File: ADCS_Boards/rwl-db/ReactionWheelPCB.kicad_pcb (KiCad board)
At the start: 4 copper layers, 90.2 x 95.9 mm, 47 parts, among them J1 PC104_Connector, U1 Conn_1, U10 LM358, U2 Conn_1, U3 Controller 1, U4 Controller 2, U5 Controller 3, U6 Controller 4, U7 Conn_1, U8 Conn_1, U9 LM358

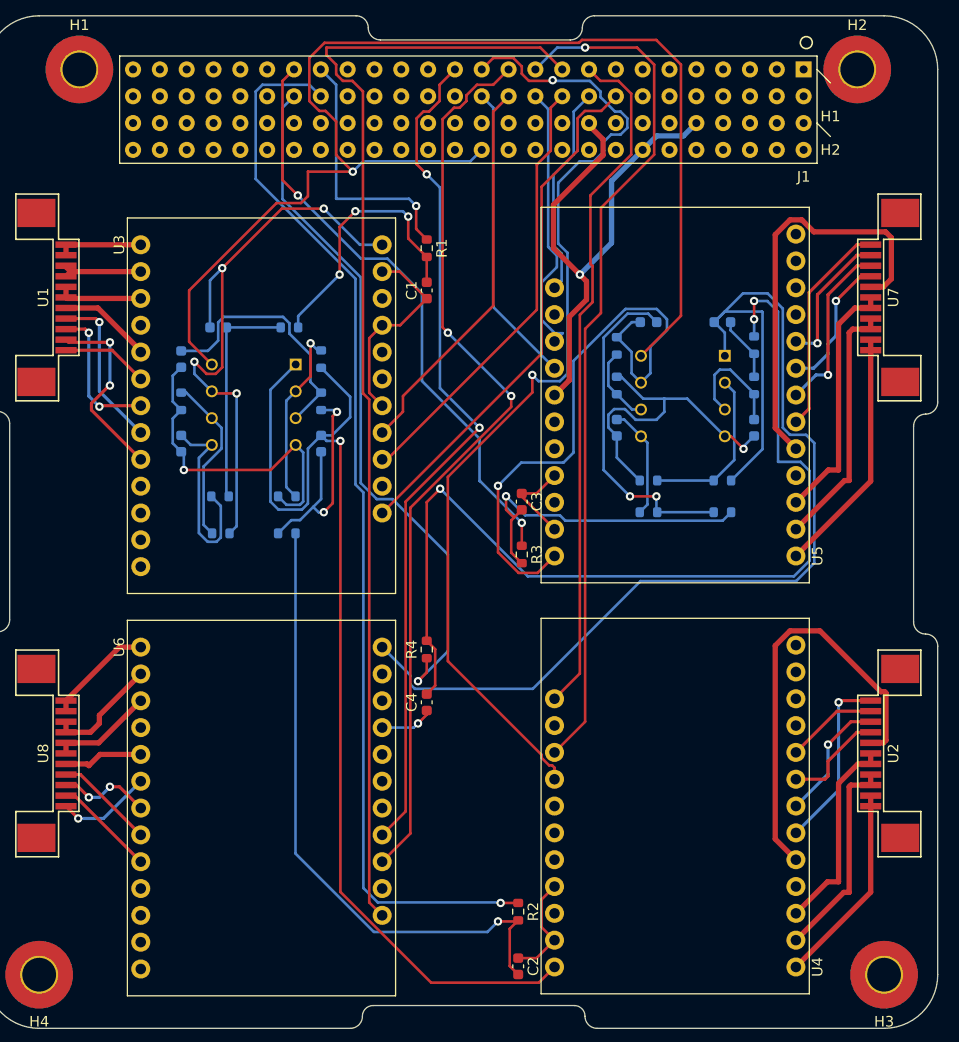
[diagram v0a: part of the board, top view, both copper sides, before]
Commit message: adcs: udpated rwl-db and adcs-ctl on behalf of Yasin
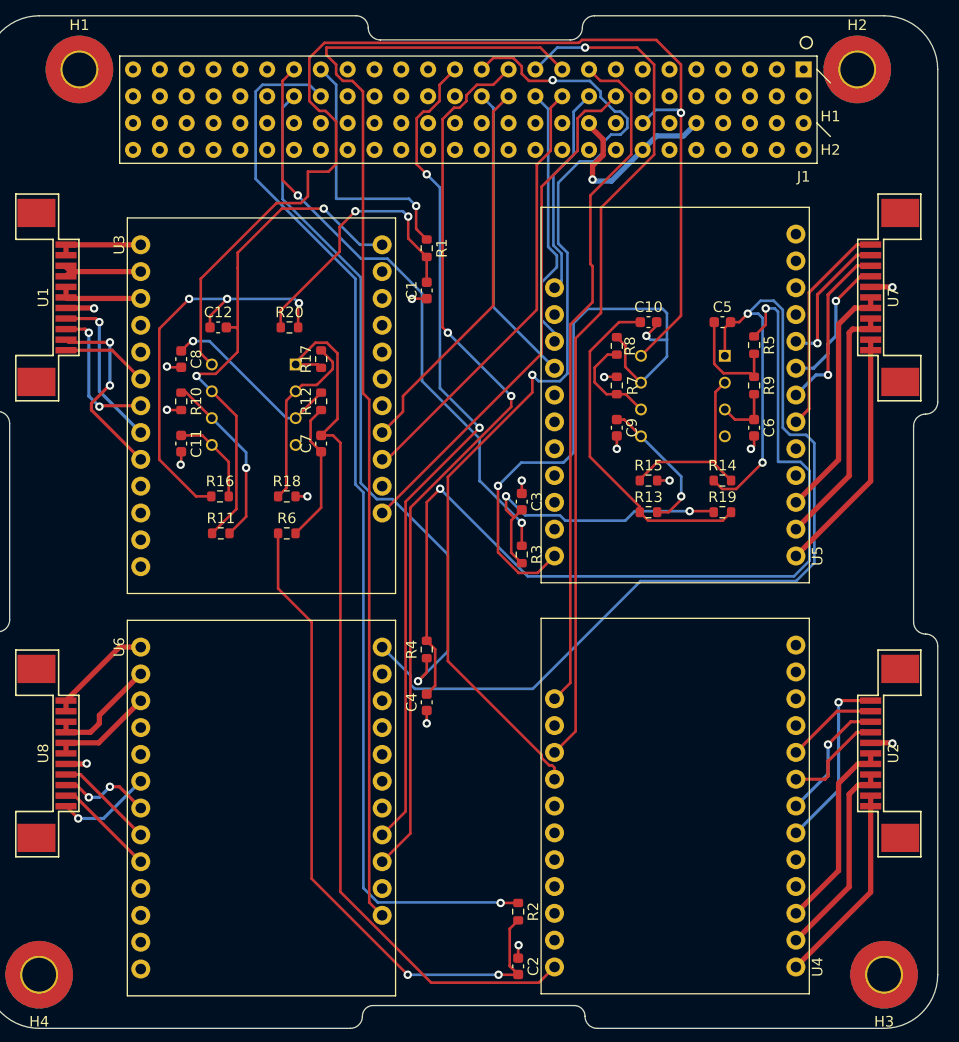
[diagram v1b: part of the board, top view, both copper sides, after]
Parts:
- C1, C2, C3, C4: value 10n -> 10nF
- C10, C11, C12, C5, C6, C7, C8, C9: value C -> 10nF; moved to F.Cu
- R10, R11, R12, R13, R14, R15, R16, R17, R18, R19, R20, R5, R6, R7, R8, R9: value R -> 10k; moved to F.Cu
- turned C10 to 0 degrees
- turned C12 to 0 degrees
- turned C5 to 0 degrees
- turned R11 to 0 degrees
- turned R13 to 0 degrees
- turned R14 to 0 degrees
- turned R15 to 0 degrees
- turned R16 to 0 degrees
- turned R18 to 0 degrees
- turned R19 to 0 degrees
- turned R20 to 0 degrees
- turned R6 to 0 degrees
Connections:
- J1 pad 65: unconnected-(J1-Pad65) -> +5V
- J1 pad 78: +5V -> unconnected-(J1-Pad78)
- J1 pad 79: +3.3V -> unconnected-(J1-Pad79)
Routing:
- net GND: track 253.5 -> 42.9 mm, vias 4 -> 17
- net RampControl(S2)_Out: track 103.5 -> 85.4 mm, vias 1 -> 0
- net Net-(C12-Pad1): track 21.2 -> 39.0 mm, vias 0 -> 3
- net +5V: track 121.3 -> 108.9 mm
- net Net-(C11-Pad1): track 19.0 -> 8.81 mm
- net Net-(C7-Pad1): track 22.7 -> 13.5 mm, vias 2 -> 0
- net RampControl(S1)_Out: track 57.2 -> 49.6 mm, vias 4 -> 2
- net Net-(C8-Pad1): track 24.1 -> 17.7 mm, vias 0 -> 1
- net Net-(C6-Pad1): track 11.0 -> 5.57 mm
- net Net-(C5-Pad1): track 6.10 -> 10.4 mm
- net RampControl(S3)_Out: track 56.6 -> 60.1 mm, vias 1 -> 2
- net RampControl(S4)_Out: track 108.2 -> 104.9 mm, vias 0 -> 2
- net Net-(C9-Pad1): track 10.7 -> 13.3 mm, vias 0 -> 1
- net RampControl(S2)_RC: track 60.7 -> 63.3 mm, vias 1 -> 2
- net Net-(R14-Pad2): track 15.8 -> 18.2 mm
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
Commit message: adcs: rwl-db: finish layout for controllers 3 and 4
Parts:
- removed U10, U9: LM358, Footprints_QSAT:DIP794W45P254L959H508Q8
- removed U7, U8: Conn_1, Footprints_QSAT:FPC_11_SAT_1-84953-1
- added J2: Conn_1, qset-footprints:FPC_11_SAT_1-84953-1, F.Cu at (119.1, 71.9)
- added J3: Conn_2, qset-footprints:FPC_11_SAT_1-84953-1, F.Cu at (190.8, 71.9)
- added J4: Conn_3, qset-footprints:FPC_11_SAT_1-84953-1, F.Cu at (119.1, 117.9)
- added J5: Conn_4, qset-footprints:FPC_11_SAT_1-84953-1, F.Cu at (190.5, 117.6)
- J1: footprint pc104-connector:pc104-connector -> qset-footprints:pc104-connector
- U1: value Conn_1 -> Controller 1; footprint Footprints_QSAT:FPC_11_SAT_1-84953-1 -> qset-footprints:Escon24.2
- U2: value Conn_1 -> Controller 2; footprint Footprints_QSAT:FPC_11_SAT_1-84953-1 -> qset-footprints:Escon24.2
- U3: value Controller 1 -> Controller 3; footprint Footprints_QSAT:Escon24.2 -> qset-footprints:Escon24.2
- U4: value Controller 2 -> Controller 4; footprint Footprints_QSAT:Escon24.2 -> qset-footprints:Escon24.2
- U5: value Controller 3 -> LM358; footprint Footprints_QSAT:Escon24.2 -> qset-footprints:DIP794W45P254L959H508Q8
- U6: value Controller 4 -> LM358; footprint Footprints_QSAT:Escon24.2 -> qset-footprints:DIP794W45P254L959H508Q8
- moved C8 255.2 mm to (383.0, 77.5), turned to 0 degrees
- moved R10 251.3 mm to (379.0, 90.0), turned to 0 degrees
- moved R11 240.2 mm to (370.9, 77.5)
- moved R6 237.9 mm to (375.0, 77.5)
- moved C1 236.0 mm to (387.0, 77.5), turned to 0 degrees
- moved U5 235.3 mm to (403.4, 4.78), turned to 0 degrees
- moved R12 226.0 mm to (366.9, 90.0), turned to 0 degrees
- moved C7 226.0 mm to (366.9, 85.0), turned to 0 degrees
- moved R1 221.0 mm to (370.9, 90.0), turned to 0 degrees
- moved R2 219.8 mm to (375.0, 87.5), turned to 0 degrees
- moved R8 218.0 mm to (387.0, 80.0), turned to 0 degrees
- moved U1 216.4 mm to (331.9, 97.4), turned to 90 degrees
- moved C2 215.0 mm to (366.9, 80.0), turned to 0 degrees
- moved R7 202.0 mm to (370.9, 87.5), turned to 0 degrees
- moved R9 201.0 mm to (383.0, 80.0), turned to 0 degrees
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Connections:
- net RampControl(S1) renamed RampControl(S1)_IN
- net RampControl(S2) renamed RampControl(S2)_IN
- net RampControl(S3) renamed RampControl(S3)_IN
- net RampControl(S4) renamed RampControl(S4)_IN
- C10 pad 2: RampControl(S3)_Out -> GND
- C11 pad 1: Net-(C11-Pad1) -> RampControl(S3)_Out
- C11 pad 2: GND -> Net-(C11-Pad2)
- C12 pad 1: Net-(C12-Pad1) -> RampControl(S4)_Out
- C12 pad 2: RampControl(S1)_Out -> Net-(C12-Pad2)
- C5 pad 1: Net-(C5-Pad1) -> GND
- C5 pad 2: RampControl(S4)_Out -> Net-(C5-Pad2)
- C7 pad 1: Net-(C7-Pad1) -> RampControl(S1)_Out
- C7 pad 2: RampControl(S2)_Out -> Net-(C7-Pad2)
- C8 pad 1: Net-(C8-Pad1) -> RampControl(S2)_Out
- C8 pad 2: GND -> Net-(C8-Pad2)
- C9 pad 1: Net-(C9-Pad1) -> GND
- C9 pad 2: GND -> Net-(C9-Pad2)
- J1 pad 84: GND -> unconnected-(J1-Pad84)
- R11 pad 1: RampControl(S1)_Out -> RampControl(S2)_Out
- R11 pad 2: Net-(R10-Pad1) -> Net-(R11-Pad2)
- R12 pad 1: Net-(C7-Pad1) -> Net-(R11-Pad2)
- R12 pad 2: Net-(C8-Pad1) -> GND
- R13 pad 1: Net-(C10-Pad1) -> Net-(C11-Pad2)
- R13 pad 2: Net-(C9-Pad1) -> RampControl(S3)_RC
- R14 pad 1: RampControl(S4)_Out -> RampControl(S4)_RC
- R14 pad 2: Net-(R14-Pad2) -> Net-(C12-Pad2)
- R15 pad 1: Net-(R14-Pad2) -> Net-(C9-Pad2)
- R15 pad 2: GND -> Net-(C11-Pad2)
- R16 pad 1: Net-(C12-Pad1) -> Net-(C12-Pad2)
- R16 pad 2: Net-(C11-Pad1) -> Net-(C10-Pad1)
- R17 pad 1: RampControl(S2)_Out -> RampControl(S3)_Out
- R19 pad 1: RampControl(S3)_RC -> RampControl(S4)_Out
- R19 pad 2: Net-(C10-Pad1) -> Net-(R19-Pad2)
- R20 pad 1: RampControl(S1)_RC -> Net-(R19-Pad2)
- R20 pad 2: Net-(C12-Pad1) -> GND
- R5 pad 1: RampControl(S4)_RC -> Net-(C7-Pad2)
- R5 pad 2: Net-(C5-Pad1) -> RampControl(S1)_RC
- R6 pad 2: Net-(C7-Pad1) -> Net-(C8-Pad2)
- R7 pad 1: Net-(R7-Pad1) -> Net-(C5-Pad2)
- R7 pad 2: GND -> Net-(C7-Pad2)
- R8 pad 1: RampControl(S3)_Out -> Net-(C8-Pad2)
- R8 pad 2: Net-(R7-Pad1) -> Net-(C6-Pad1)
- R9 pad 1: Net-(C5-Pad1) -> RampControl(S1)_Out
- R9 pad 2: Net-(C6-Pad1) -> Net-(R10-Pad1)
- U1 pad 10: Net-(U1-Pad10) -> unconnected-(U1-Pad10)
- U1 pad 11: Net-(U1-Pad10) -> unconnected-(U1-Pad11)
- U1 pad 4: Net-(U1-Pad4) -> +12V
- U1 pad 7: Net-(U1-Pad6) -> Net-(U1-Pad7)
- U1 pad 9: Net-(U1-Pad8) -> Net-(U1-Pad9)
- U2 pad 10: Net-(U2-Pad10) -> unconnected-(U2-Pad10)
- U2 pad 11: Net-(U2-Pad10) -> unconnected-(U2-Pad11)
- U2 pad 4: Net-(U2-Pad4) -> +12V
- U2 pad 7: Net-(U2-Pad6) -> Net-(U2-Pad7)
- U2 pad 9: Net-(U2-Pad8) -> Net-(U2-Pad9)
- U3 pad 1: Net-(U1-Pad10) -> Net-(U3-Pad1)
- U3 pad 14: Enable(S1) -> Enable(S3)
- U3 pad 16: Direction(S1) -> Direction(S3)
- U3 pad 17: PWM-SetValue(S1) -> PWM-SetValue(S3)
- U3 pad 2: Net-(U1-Pad8) -> Net-(U3-Pad2)
- U3 pad 24: RampControl(S1)_Out -> RampControl(S3)_Out
- U3 pad 3: Net-(U1-Pad6) -> Net-(U3-Pad3)
- U3 pad 6: Net-(U1-Pad1) -> Net-(U3-Pad6)
- U3 pad 7: Net-(U1-Pad3) -> Net-(U3-Pad7)
- U3 pad 8: Net-(U1-Pad4) -> Net-(U3-Pad8)
- U3 pad 9: Net-(U1-Pad2) -> Net-(U3-Pad9)
- U4 pad 1: Net-(U2-Pad10) -> Net-(U4-Pad1)
- U4 pad 14: Enable(S2) -> Enable(S4)
- U4 pad 16: Direction(S2) -> Direction(S4)
- U4 pad 17: PWM-SetValue(S2) -> PWM-SetValue(S4)
- U4 pad 2: Net-(U2-Pad8) -> Net-(U4-Pad2)
- U4 pad 24: RampControl(S2)_Out -> RampControl(S4)_Out
- U4 pad 3: Net-(U2-Pad6) -> Net-(U4-Pad3)
- U4 pad 6: Net-(U2-Pad1) -> Net-(U4-Pad6)
- U4 pad 7: Net-(U2-Pad3) -> Net-(U4-Pad7)
- U4 pad 8: Net-(U2-Pad4) -> Net-(U4-Pad8)
- U4 pad 9: Net-(U2-Pad2) -> Net-(U4-Pad9)
- U5 pad 1: Net-(U5-Pad1) -> RampControl(S1)_Out
- U5 pad 2: Net-(U5-Pad2) -> Net-(R10-Pad1)
- U5 pad 3: Net-(U5-Pad3) -> Net-(C5-Pad2)
- U5 pad 4: +12V -> GND
- U5 pad 5: GND -> Net-(C6-Pad1)
- U5 pad 6: Net-(U5-Pad6) -> Net-(R11-Pad2)
- U5 pad 7: Net-(U5-Pad7) -> RampControl(S2)_Out
- U5 pad 8: Net-(U5-Pad8) -> +5V
- U6 pad 1: Net-(U6-Pad1) -> RampControl(S3)_Out
- U6 pad 2: Net-(U6-Pad2) -> Net-(R17-Pad2)
- U6 pad 3: Net-(U6-Pad3) -> Net-(C9-Pad2)
- U6 pad 4: +12V -> GND
- U6 pad 5: GND -> Net-(C10-Pad1)
- U6 pad 6: Net-(U6-Pad6) -> Net-(R19-Pad2)
- U6 pad 7: Net-(U6-Pad7) -> RampControl(S4)_Out
- U6 pad 8: Net-(U6-Pad8) -> +5V
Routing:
- net +5V: track 108.9 -> 1.18 mm
- net RampControl(S2)_IN: track 101.8 -> 0.00 mm, vias 1 -> 0
- net Enable(S4): track 108.1 -> 10.4 mm
- net PWM-SetValue(S2): track 95.8 -> 0.00 mm, vias 2 -> 0
- net RampControl(S4)_RC: track 90.5 -> 3.03 mm, vias 2 -> 0
- net RampControl(S2)_Out: track 85.4 -> 0.00 mm
- net Direction(S2): track 81.8 -> 0.00 mm, vias 1 -> 0
- net RampControl(S4)_Out: track 104.9 -> 31.6 mm, vias 2 -> 0
- net Direction(S4): track 86.6 -> 17.4 mm, vias 2 -> 0
- net Enable(S2): track 65.4 -> 0.00 mm
- net RampControl(S2)_RC: track 63.3 -> 0.00 mm, vias 2 -> 0
- net PWM-SetValue(S4): track 80.6 -> 21.6 mm, vias 2 -> 0
- net RampControl(S4)_IN: track 66.9 -> 12.5 mm, vias 1 -> 0
- net RampControl(S1)_Out: track 49.6 -> 0.00 mm, vias 2 -> 0
- net Enable(S1): track 49.5 -> 0.00 mm
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
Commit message: adcs: rwl-db: finish layout of controllers 1 and 2
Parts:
- added G***: LOGO, LOGO, F.Cu at (117.3, 94.7)
- moved U5 263.8 mm to (154.9, 93.5)
- moved C1 234.5 mm to (152.6, 70.6), turned to -90 degrees
- moved R9 230.4 mm to (152.6, 80.5), turned to -90 degrees
- moved R8 228.8 mm to (158.2, 82.8), turned to 180 degrees
- moved R10 228.1 mm to (151.1, 80.5), turned to 90 degrees
- moved R5 227.2 mm to (151.9, 72.9)
- moved C5 227.1 mm to (151.9, 84.3)
- moved C8 224.8 mm to (158.2, 74.4)
- moved R1 220.7 mm to (151.1, 70.6), turned to -90 degrees
- moved R7 219.1 mm to (151.9, 82.8), turned to 180 degrees
- moved R2 218.1 mm to (157.5, 70.6), turned to -90 degrees
- moved R6 216.8 mm to (158.2, 72.9)
- moved C7 215.3 mm to (151.9, 74.4), turned to 180 degrees
- moved R11 213.5 mm to (157.5, 80.5), turned to -90 degrees
- moved U1 212.5 mm to (122.1, 64.1)
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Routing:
- net PWM-SetValue(S4): track 21.6 -> 101.8 mm
- net Direction(S1): track 0.00 -> 77.8 mm
- net Enable(S3): track 33.6 -> 110.9 mm, vias 0 -> 1
- net Direction(S4): track 17.4 -> 93.6 mm, vias 0 -> 1
- net Enable(S1): track 0.00 -> 73.1 mm, vias 0 -> 1
- net Enable(S4): track 10.4 -> 80.1 mm, vias 0 -> 1
- net Direction(S3): track 27.4 -> 94.2 mm, vias 0 -> 1
- net RampControl(S3)_IN: track 12.7 -> 75.4 mm, vias 0 -> 1
- net RampControl(S4)_IN: track 12.5 -> 74.8 mm, vias 0 -> 1
- net PWM-SetValue(S3): track 24.0 -> 82.4 mm, vias 0 -> 1
- net PWM-SetValue(S1): track 0.00 -> 50.5 mm
- net PWM-SetValue(S2): track 0.00 -> 47.0 mm, vias 0 -> 1
- net Direction(S2): track 0.00 -> 45.8 mm
- net RampControl(S1)_Out: track 0.00 -> 36.2 mm
- net RampControl(S2)_Out: track 0.00 -> 31.4 mm
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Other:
- board text added: "RWL-DB-REVA"
- board text added: "SN: ___________"
- board text added: "Yasin Shahrami Davis Edward Cal Graham Alex Bartley Aidan Sheedy"

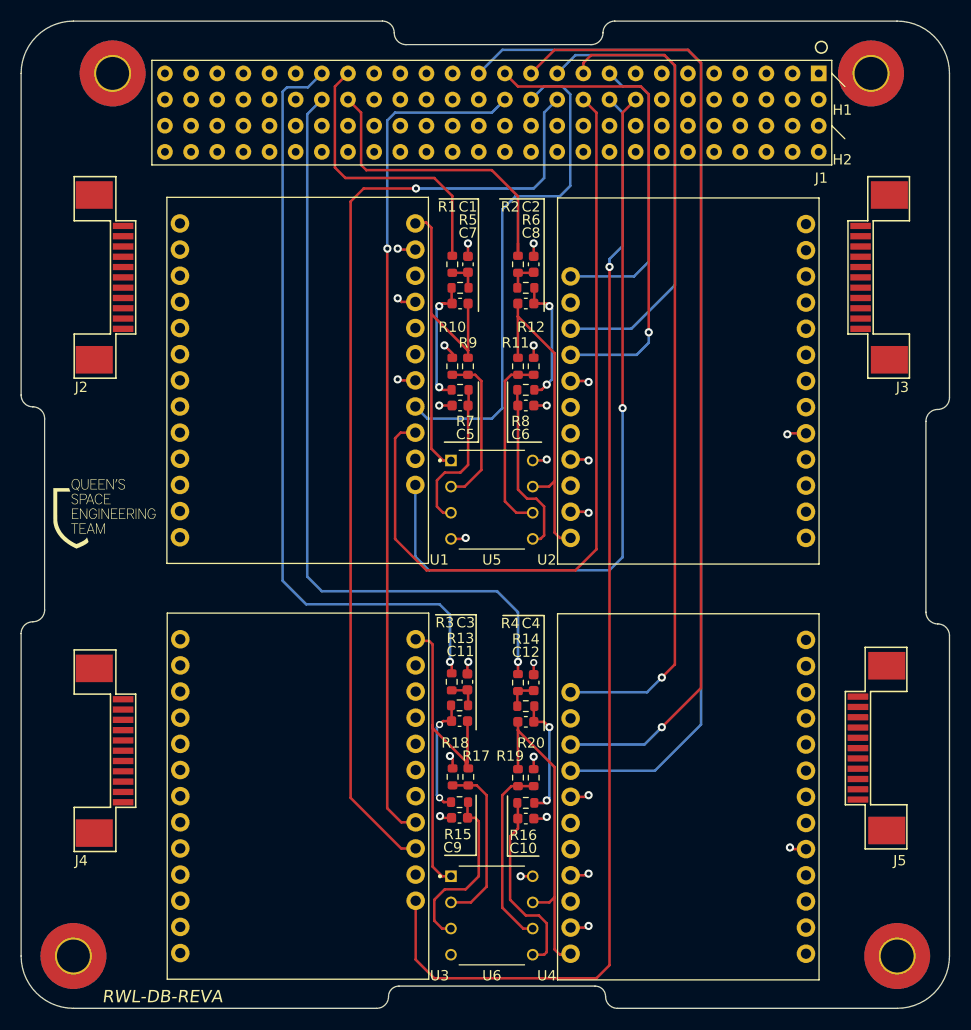
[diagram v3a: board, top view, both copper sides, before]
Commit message: adcs: Updated rw-db with latest PWM filter design and added misc silkscreen
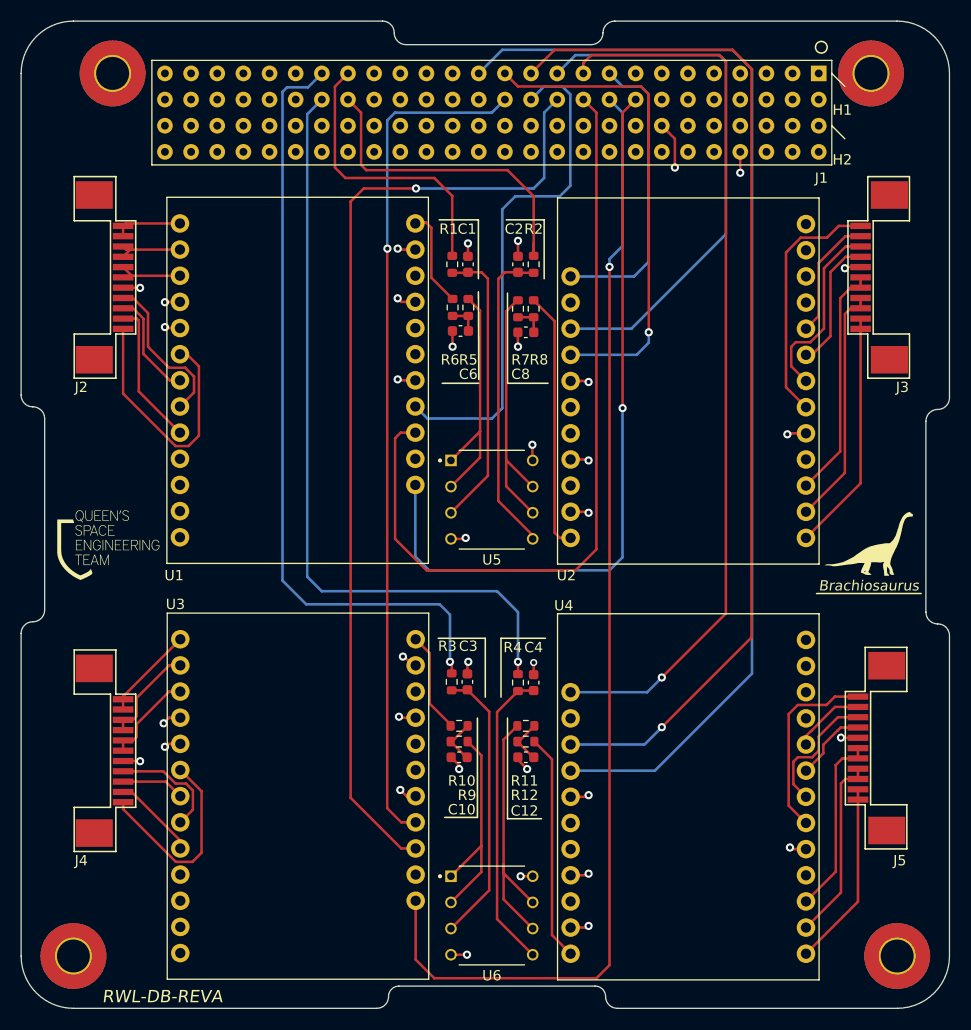
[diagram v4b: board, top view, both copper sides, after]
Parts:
- removed C11, C5, C7, C9: 10nF, Capacitor_SMD:C_0603_1608Metric
- removed R13, R14, R15, R16, R17, R18, R19, R20: 10k, Resistor_SMD:R_0603_1608Metric
- added Brachiosaurus: LOGO, LOGO, F.Cu at (192.3, 97.8)
- moved R9 36.5 mm to (151.8, 117.0), turned to 0 degrees
- moved R12 36.5 mm to (158.2, 117.0), turned to 0 degrees
- moved R11 34.9 mm to (158.2, 115.4), turned to 0 degrees
- moved R10 34.9 mm to (151.8, 115.4), turned to 0 degrees
- moved R7 9.67 mm to (157.5, 74.9), turned to -90 degrees
- moved C6 9.63 mm to (151.9, 77.1)
- moved C10 8.80 mm to (151.8, 118.5)
- moved R8 7.91 mm to (159.0, 74.9), turned to -90 degrees
- moved R6 7.36 mm to (151.1, 74.8), turned to -90 degrees
- moved C12 3.44 mm to (158.2, 118.5)
- moved G*** 3.07 mm to (117.7, 97.8)
- moved C8 2.79 mm to (158.2, 77.2)
- moved R5 2.06 mm to (152.7, 74.8), turned to 90 degrees
- moved C2 1.52 mm to (157.5, 70.6)
- moved R2 1.52 mm to (159.0, 70.6)
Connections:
- C10 pad 1: Net-(C10-Pad1) -> GND
- C10 pad 2: GND -> Net-(C10-Pad2)
- C12 pad 1: RampControl(S4)_Out -> GND
- C6 pad 1: Net-(C6-Pad1) -> GND
- C6 pad 2: GND -> Net-(C6-Pad2)
- C8 pad 1: RampControl(S2)_Out -> GND
- R10 pad 1: Net-(R10-Pad1) -> RampControl(S3)_Out
- R10 pad 2: GND -> Net-(C10-Pad2)
- R11 pad 1: RampControl(S2)_Out -> Net-(R11-Pad1)
- R11 pad 2: Net-(R11-Pad2) -> Net-(C12-Pad2)
- R12 pad 1: Net-(R11-Pad2) -> Net-(C12-Pad2)
- R12 pad 2: GND -> RampControl(S4)_Out
- R5 pad 1: Net-(C7-Pad2) -> Net-(C6-Pad2)
- R5 pad 2: RampControl(S1)_RC -> Net-(R5-Pad2)
- R6 pad 1: RampControl(S2)_RC -> RampControl(S1)_Out
- R6 pad 2: Net-(C8-Pad2) -> Net-(C6-Pad2)
- R7 pad 1: Net-(C5-Pad2) -> Net-(R7-Pad1)
- R7 pad 2: Net-(C7-Pad2) -> Net-(C8-Pad2)
- R8 pad 2: Net-(C6-Pad1) -> RampControl(S2)_Out
- R9 pad 1: RampControl(S1)_Out -> Net-(C10-Pad2)
- R9 pad 2: Net-(R10-Pad1) -> Net-(R9-Pad2)
- U5 pad 1: RampControl(S1)_Out -> Net-(R5-Pad2)
- U5 pad 2: Net-(R10-Pad1) -> Net-(R5-Pad2)
- U5 pad 3: Net-(C5-Pad2) -> RampControl(S1)_RC
- U5 pad 5: Net-(C6-Pad1) -> RampControl(S2)_RC
- U5 pad 6: Net-(R11-Pad2) -> Net-(R7-Pad1)
- U5 pad 7: RampControl(S2)_Out -> Net-(R7-Pad1)
- U6 pad 1: RampControl(S3)_Out -> Net-(R9-Pad2)
- U6 pad 2: Net-(R17-Pad2) -> Net-(R9-Pad2)
- U6 pad 3: Net-(C9-Pad2) -> RampControl(S3)_RC
- U6 pad 5: Net-(C10-Pad1) -> RampControl(S4)_RC
- U6 pad 6: Net-(R19-Pad2) -> Net-(R11-Pad1)
- U6 pad 7: RampControl(S4)_Out -> Net-(R11-Pad1)
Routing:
- net RampControl(S2)_RC: track 3.03 -> 30.4 mm
- net RampControl(S1)_Out: track 36.2 -> 9.58 mm
- net RampControl(S4)_RC: track 3.03 -> 29.4 mm
- net Net-(R11-Pad1): track 0.00 -> 26.4 mm
- net RampControl(S3)_Out: track 35.8 -> 9.78 mm
- net Net-(R7-Pad1): track 0.00 -> 25.9 mm
- net Net-(U1-Pad6): track 0.00 -> 25.2 mm
- net RampControl(S1)_RC: track 3.08 -> 28.0 mm
- net Net-(U2-Pad6): track 0.00 -> 24.1 mm
- net RampControl(S3)_RC: track 3.08 -> 27.1 mm
- net Net-(R5-Pad2): track 0.00 -> 24.1 mm
- net Net-(U2-Pad2): track 0.00 -> 23.5 mm
- net Net-(U2-Pad1): track 0.00 -> 23.5 mm
- net Net-(U2-Pad3): track 0.00 -> 23.0 mm
- net Net-(R9-Pad2): track 0.00 -> 21.6 mm
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- added copper zone on In2.Cu, net +5V
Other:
- board text added: "Brachiosaurus"
